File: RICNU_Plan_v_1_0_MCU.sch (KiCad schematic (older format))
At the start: 63 parts, among them SW3 SW_Push, U8 STM32F103RC, Y1 Crystal

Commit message: Re-routed CAN, RS-485, and debug connectors (wrong polarity in all)
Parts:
- removed SW3: SW_Push, Buttons_Switches_SMD:SW_SPST_KMR2, symbol SW_Push
- added SW3: SW_Push_4pin, RICNU_Plan_v_1_0:SW_SPST_KMR7, symbol SW_Push_4pin
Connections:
- net GND: now also SW3.2
- net MCU.CAN.SHDN: now also U8.8 (PC0); no longer U8.60 (BOOT0)
- net MCU.CAN.STB: now also U8.60 (BOOT0); no longer U8.8 (PC0)
- net MCU_SWD_RESET: now also SW3.1
- no-connect marks 9 -> 11
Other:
- moved on the sheet: C15

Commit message: Added connections to monitor power, changed CANSTB MCU pin, moved LED pins around
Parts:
- added R92: 10k, Resistors_SMD:R_0402_NoSilk, symbol R
- added R93, R94: 180, Resistors_SMD:R_0402_NoSilk, symbol R
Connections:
- net GND: now also R92.2
- net MCU.CAN.STB: now also U8.9 (PC1); no longer U8.60 (BOOT0)
- net MCU.LED.1: now also U8.15 (PA1); no longer U8.9 (PC1)
- net MCU.LED.2: now also U8.26 (PB0); no longer U8.10 (PC2)
- net MCU.LED.3: now also U8.27 (PB1); no longer U8.11 (PC3)
- net MCU.LED.4: now also U8.28 (PB2); no longer U8.15 (PA1)
- net MCU_PWREN: now reaches U8.39 (PC8)
- net MCU_PWREN: now also R93.2
- net MCU_USBON: now reaches U8.40 (PC9)
- net MCU_USBON: now also R92.1, R94.2
- new net MCU.PWREN: R93.1
- new net MCU.USBON: R94.1
- no-connect marks 11 -> 9
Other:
- note added: "USB Power Status Inputs"
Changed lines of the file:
@@
 Text HLabel 1650 4650 0    60   Output ~ 0
 MCU.RS485.TX
-NoConn ~ 6450 3400
-NoConn ~ 4950 3500
-NoConn ~ 4950 3600
-NoConn ~ 4950 3700
 NoConn ~ 4950 3400
 NoConn ~ 4950 1100
-NoConn ~ 6450 3500
 Text HLabel 10650 5050 2    60   BiDi ~ 0
 MCU.PB11
@@
 Text Label 2750 5900 0    60   ~ 0
 MCU_CAN_STB
-Text Label 6850 1400 0    60   ~ 0
+Text Label 4550 1800 2    60   ~ 0
 MCU_CAN_STB
 Text Label 2750 6000 0    60   ~ 0
@@
 Text Notes 900  1150 0    60   ~ 0
 SPI to SD Card
-Text Label 4550 1800 2    60   ~ 0
+Text Label 4550 2400 2    60   ~ 0
 MCU_LED_1
-Text Label 4550 1900 2    60   ~ 0
+Text Label 4550 3500 2    60   ~ 0
 MCU_LED_2
-Text Label 4550 2000 2    60   ~ 0
+Text Label 4550 3600 2    60   ~ 0
 MCU_LED_3
-Text Label 4550 2400 2    60   ~ 0
+Text Label 4550 3700 2    60   ~ 0
 MCU_LED_4
 $Comp
@@
 Text Label 4550 3900 2    60   ~ 0
 MCU_DIO_PB11
-Text HLabel 10300 3000 2    60   Input ~ 0
+Text HLabel 10300 2550 2    60   Input ~ 0
 MCU.LED.1
-Text HLabel 10300 3100 2    60   Input ~ 0
+Text HLabel 10300 2650 2    60   Input ~ 0
 MCU.LED.2
-Text HLabel 10300 3200 2    60   Input ~ 0
+Text HLabel 10300 2750 2    60   Input ~ 0
 MCU.LED.3
-Text HLabel 10300 3300 2    60   Input ~ 0
+Text HLabel 10300 2850 2    60   Input ~ 0
 MCU.LED.4
 $Comp
@@
 Text Label 8450 5050 2    60   ~ 0
 MCU_DIO_PB11
-Text Label 9200 3000 2    60   ~ 0
+Text Label 9200 2550 2    60   ~ 0
 MCU_LED_1
-Text Label 9200 3100 2    60   ~ 0
+Text Label 9200 2650 2    60   ~ 0
 MCU_LED_2
-Text Label 9200 3200 2    60   ~ 0
+Text Label 9200 2750 2    60   ~ 0
 MCU_LED_3
-Text Label 9200 3300 2    60   ~ 0
+Text Label 9200 2850 2    60   ~ 0
 MCU_LED_4
 $Comp
@@
 Text Notes 11100 4600 2    60   ~ 0
 GPIO Breakout
-Text Notes 10850 2850 2    60   ~ 0
+Text Notes 10850 2400 2    60   ~ 0
 LED Controls
 Text Label 4950 1200 2    60   ~ 0
@@
 Wire Wire Line
 	4550 1800 4950 1800
-Wire Wire Line
-	4550 1900 4950 1900
-Wire Wire Line
-	4550 2000 4950 2000
 Wire Notes Line
 	10500 1450 10500 2100
@@
 	10500 6250 10650 6250
 Wire Wire Line
-	10300 3000 9200 3000
-Wire Wire Line
-	10300 3100 9200 3100
-Wire Wire Line
-	10300 3200 9200 3200
-Wire Wire Line
-	10300 3300 9200 3300
+	10300 2550 9200 2550
+Wire Wire Line
+	10300 2650 9200 2650
+Wire Wire Line
+	10300 2750 9200 2750
+Wire Wire Line
+	10300 2850 9200 2850
 Wire Wire Line
 	8500 4400 8500 4250
@@
 Wire Wire Line
 	9850 4400 9850 4250
-Wire Wire Line
-	6450 1400 6850 1400
 Wire Wire Line
 	4550 2400 4950 2400
@@
 NoConn ~ 4900 5600
 NoConn ~ 4900 5200
+NoConn ~ 6450 1400
+Wire Wire Line
+	4950 3500 4550 3500
+Wire Wire Line
+	4950 3600 4550 3600
+Wire Wire Line
+	4950 3700 4550 3700
+NoConn ~ 4950 1900
+NoConn ~ 4950 2000
+Wire Wire Line
+	6450 3500 6850 3500
+Text Label 6850 3500 0    60   ~ 0
+MCU_PWREN
+Text Label 9200 3200 2    60   ~ 0
+MCU_PWREN
+Text HLabel 10300 3200 2    60   Input ~ 0
+MCU.PWREN
+Text Notes 10850 3100 2    60   ~ 0
+USB Power Status Inputs
+$Comp
+L R R93
+U 1 1 5A214822
+P 9750 3200
+F 0 "R93" V 9800 3400 50  0000 C CNN
+F 1 "180" V 9750 3200 50  0000 C CNN
+F 2 "Resistors_SMD:R_0402_NoSilk" V 9680 3200 50  0001 C CNN
+F 3 "" H 9750 3200 50  0001 C CNN
+	1    9750 3200
+	0    1    1    0
+$EndComp
+Wire Wire Line
+	9900 3200 10300 3200
+Wire Wire Line
+	9600 3200 9200 3200
+Text HLabel 10300 3300 2    60   Input ~ 0
+MCU.USBON
+Wire Wire Line
+	10300 3300 9900 3300
+$Comp
+L R R94
+U 1 1 5A2157A3
+P 9750 3300
+F 0 "R94" V 9800 3500 50  0000 C CNN
+F 1 "180" V 9750 3300 50  0000 C CNN
+F 2 "Resistors_SMD:R_0402_NoSilk" V 9680 3300 50  0001 C CNN
+F 3 "" H 9750 3300 50  0001 C CNN
+	1    9750 3300
+	0    1    1    0
+$EndComp
+Wire Wire Line
+	9600 3300 9200 3300
+Text Label 6850 3400 0    60   ~ 0
+MCU_USBON
+Wire Wire Line
+	6450 3400 6850 3400
+$Comp
+L R R92
+U 1 1 5A216900
+P 9400 3550
+F 0 "R92" V 9450 3750 50  0000 C CNN
+F 1 "10k" V 9400 3550 50  0000 C CNN
+F 2 "Resistors_SMD:R_0402_NoSilk" V 9330 3550 50  0001 C CNN
+F 3 "" H 9400 3550 50  0001 C CNN
+	1    9400 3550
+	1    0    0    -1
+$EndComp
+Wire Wire Line
+	9400 3400 9400 3300
+Connection ~ 9400 3300
+Wire Wire Line
+	9400 3700 9400 3800
+$Comp
+L GND #PWR057
+U 1 1 5A217257
+P 9400 3800
+F 0 "#PWR057" H 9400 3550 50  0001 C CNN
+F 1 "GND" H 9400 3650 50  0000 C CNN
+F 2 "" H 9400 3800 50  0001 C CNN
+F 3 "" H 9400 3800 50  0001 C CNN
+	1    9400 3800
+	-1   0    0    -1
+$EndComp
+Text Label 9200 3300 2    60   ~ 0
+MCU_USBON
 $EndSCHEMATC

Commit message: Design freeze - ordered the board
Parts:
- added R96, R99: 470, Resistors_SMD:R_0402_NoSilk, symbol R
- added R97, R98: 10k, Resistors_SMD:R_0402_NoSilk, symbol R
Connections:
- net +3V3: now also R97.1, R98.1
- net GND: now also R96.2, R99.2
- net MCU.LED.1: now also U8.25 (PC5); no longer U8.15 (PA1)
- net MCU.LED.4: now also U8.15 (PA1); no longer U8.28 (PB2)
- net MCU_BOOT0: now reaches U8.60 (BOOT0)
- net MCU_BOOT0: now also R98.2, R99.1
- new net MCU_BOOT1: R96.1, R97.2, U8.28 (PB2)
- no-connect marks 9 -> 7
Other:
- note added: "DNP"
- moved on the sheet: C13, C14, Y1
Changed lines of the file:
@@
 L Crystal Y1
 U 1 1 59D7EC04
-P 4200 1100
-F 0 "Y1" H 4200 1250 50  0000 C CNN
-F 1 "Crystal" H 4200 950 50  0000 C CNN
-F 2 "Crystals:Crystal_SMD_3215-2pin_3.2x1.5mm" H 4200 1100 50  0001 C CNN
-F 3 "" H 4200 1100 50  0001 C CNN
-	1    4200 1100
+P 4100 1100
+F 0 "Y1" H 4100 1250 50  0000 C CNN
+F 1 "Crystal" H 4100 950 50  0000 C CNN
+F 2 "Crystals:Crystal_SMD_3215-2pin_3.2x1.5mm" H 4100 1100 50  0001 C CNN
+F 3 "" H 4100 1100 50  0001 C CNN
+	1    4100 1100
 	0    1    1    0
 $EndComp
@@
 L C C13
 U 1 1 59D7EC93
-P 4000 900
-F 0 "C13" H 4025 1000 50  0000 L CNN
-F 1 "7p" H 4025 800 50  0000 L CNN
-F 2 "Capacitors_SMD:C_0402_NoSilk" H 4038 750 50  0001 C CNN
-F 3 "" H 4000 900 50  0001 C CNN
-	1    4000 900
+P 3900 900
+F 0 "C13" H 3925 1000 50  0000 L CNN
+F 1 "7p" H 3925 800 50  0000 L CNN
+F 2 "Capacitors_SMD:C_0402_NoSilk" H 3938 750 50  0001 C CNN
+F 3 "" H 3900 900 50  0001 C CNN
+	1    3900 900
 	0    1    1    0
 $EndComp
@@
 L C C14
 U 1 1 59D7ECF9
-P 4000 1300
-F 0 "C14" H 4025 1400 50  0000 L CNN
-F 1 "7p" H 4025 1200 50  0000 L CNN
-F 2 "Capacitors_SMD:C_0402_NoSilk" H 4038 1150 50  0001 C CNN
-F 3 "" H 4000 1300 50  0001 C CNN
-	1    4000 1300
+P 3900 1300
+F 0 "C14" H 3925 1400 50  0000 L CNN
+F 1 "7p" H 3925 1200 50  0000 L CNN
+F 2 "Capacitors_SMD:C_0402_NoSilk" H 3938 1150 50  0001 C CNN
+F 3 "" H 3900 1300 50  0001 C CNN
+	1    3900 1300
 	0    1    1    0
 $EndComp
@@
 Text HLabel 1650 4650 0    60   Output ~ 0
 MCU.RS485.TX
-NoConn ~ 4950 3400
 NoConn ~ 4950 1100
 Text HLabel 10650 5050 2    60   BiDi ~ 0
@@
 L GND #PWR042
 U 1 1 59DE2264
-P 3700 1200
-F 0 "#PWR042" H 3700 950 50  0001 C CNN
-F 1 "GND" H 3700 1050 50  0000 C CNN
-F 2 "" H 3700 1200 50  0001 C CNN
-F 3 "" H 3700 1200 50  0001 C CNN
-	1    3700 1200
+P 3600 1200
+F 0 "#PWR042" H 3600 950 50  0001 C CNN
+F 1 "GND" H 3600 1050 50  0000 C CNN
+F 2 "" H 3600 1200 50  0001 C CNN
+F 3 "" H 3600 1200 50  0001 C CNN
+	1    3600 1200
 	1    0    0    -1
 $EndComp
@@
 Text Notes 900  1150 0    60   ~ 0
 SPI to SD Card
-Text Label 4550 2400 2    60   ~ 0
+Text Label 4550 3400 2    60   ~ 0
 MCU_LED_1
 Text Label 4550 3500 2    60   ~ 0
@@
 Text Label 4550 3600 2    60   ~ 0
 MCU_LED_3
-Text Label 4550 3700 2    60   ~ 0
+Text Label 4550 2400 2    60   ~ 0
 MCU_LED_4
 $Comp
@@
 Text Notes 10850 2400 2    60   ~ 0
 LED Controls
-Text Label 4950 1200 2    60   ~ 0
+Text Label 4400 1200 0    60   ~ 0
 OSC32_IN
-Text Label 4950 1300 2    60   ~ 0
+Text Label 4400 1300 0    60   ~ 0
 OSC32_OUT
 Text Label 8650 1650 0    60   ~ 0
@@
 Text Label 6850 1000 0    60   ~ 0
 MCU_VCC
-Text Label 4550 750  2    60   ~ 0
+Text Label 4400 1000 0    60   ~ 0
 MCU_VCC
 Text Label 6850 2600 0    60   ~ 0
@@
 Connection ~ 10350 2050
 Wire Wire Line
-	3800 1300 3850 1300
-Wire Wire Line
-	3850 900  3800 900
-Wire Wire Line
-	4150 900  4450 900
-Wire Wire Line
-	4200 900  4200 950
-Wire Wire Line
-	4200 1300 4200 1250
-Connection ~ 4200 900
-Connection ~ 4200 1300
+	3700 1300 3750 1300
+Wire Wire Line
+	3750 900  3700 900
+Wire Wire Line
+	4050 900  4350 900
+Wire Wire Line
+	4100 900  4100 950
+Wire Wire Line
+	4100 1300 4100 1250
+Connection ~ 4100 900
+Connection ~ 4100 1300
 Wire Wire Line
 	6450 2500 6850 2500
@@
 	4550 1600 4950 1600
 Wire Wire Line
-	3800 900  3800 1300
-Connection ~ 3800 1100
-Wire Wire Line
-	4150 1300 4950 1300
-Wire Wire Line
-	4450 1200 4950 1200
+	3700 900  3700 1300
+Connection ~ 3700 1100
+Wire Wire Line
+	4050 1300 4950 1300
+Wire Wire Line
+	4350 1200 4950 1200
 Wire Wire Line
 	6850 2400 6450 2400
@@
 	4550 3900 4950 3900
 Wire Wire Line
-	3700 1200 3700 1100
-Wire Wire Line
-	3700 1100 3800 1100
+	3600 1200 3600 1100
+Wire Wire Line
+	3600 1100 3700 1100
 Wire Wire Line
 	6850 3300 6450 3300
 Wire Wire Line
-	4450 900  4450 1200
+	4350 900  4350 1200
 Wire Wire Line
 	2200 1300 2650 1300
@@
 Wire Wire Line
 	9850 4400 9850 4250
-Wire Wire Line
-	4550 2400 4950 2400
 $Comp
 L SW_Push_4pin SW3
@@
 $EndComp
 Wire Wire Line
-	4550 750  4550 1000
-Wire Wire Line
-	4550 1000 4950 1000
+	4400 1000 4950 1000
 $Comp
 L PWR_FLAG #FLG057
@@
 NoConn ~ 4900 5600
 NoConn ~ 4900 5200
-NoConn ~ 6450 1400
 Wire Wire Line
 	4950 3500 4550 3500
@@
 $EndComp
 Wire Wire Line
-	9600 3300 9200 3300
+	9200 3300 9600 3300
 Text Label 6850 3400 0    60   ~ 0
 MCU_USBON
@@
 Text Label 9200 3300 2    60   ~ 0
 MCU_USBON
+Wire Wire Line
+	4550 3400 4950 3400
+Text Label 6850 1400 0    60   ~ 0
+MCU_BOOT0
+Text Label 4550 3700 2    60   ~ 0
+MCU_BOOT1
+Wire Wire Line
+	6450 1400 6850 1400
+Wire Wire Line
+	5500 6700 5500 6800
+$Comp
+L GND #PWR059
+U 1 1 5A25E35E
+P 5500 7150
+F 0 "#PWR059" H 5500 6900 50  0001 C CNN
+F 1 "GND" H 5500 7000 50  0000 C CNN
+F 2 "" H 5500 7150 50  0001 C CNN
+F 3 "" H 5500 7150 50  0001 C CNN
+	1    5500 7150
+	1    0    0    -1
+$EndComp
+Wire Wire Line
+	5500 7150 5500 7100
+$Comp
+L R R99
+U 1 1 5A25E365
+P 5500 6950
+F 0 "R99" V 5600 6950 50  0000 C CNN
+F 1 "470" V 5500 6950 50  0000 C CNN
+F 2 "Resistors_SMD:R_0402_NoSilk" V 5430 6950 50  0001 C CNN
+F 3 "" H 5500 6950 50  0001 C CNN
+	1    5500 6950
+	1    0    0    -1
+$EndComp
+Wire Wire Line
+	4500 6750 4350 6750
+Text Label 4350 6750 2    60   ~ 0
+MCU_BOOT1
+Text Label 5350 6750 2    60   ~ 0
+MCU_BOOT0
+Wire Wire Line
+	5350 6750 5500 6750
+$Comp
+L GND #PWR060
+U 1 1 5A25974F
+P 4500 7150
+F 0 "#PWR060" H 4500 6900 50  0001 C CNN
+F 1 "GND" H 4500 7000 50  0000 C CNN
+F 2 "" H 4500 7150 50  0001 C CNN
+F 3 "" H 4500 7150 50  0001 C CNN
+	1    4500 7150
+	1    0    0    -1
+$EndComp
+Wire Wire Line
+	4500 7150 4500 7100
+$Comp
+L R R96
+U 1 1 5A25A976
+P 4500 6950
+F 0 "R96" V 4600 6950 50  0000 C CNN
+F 1 "470" V 4500 6950 50  0000 C CNN
+F 2 "Resistors_SMD:R_0402_NoSilk" V 4430 6950 50  0001 C CNN
+F 3 "" H 4500 6950 50  0001 C CNN
+	1    4500 6950
+	1    0    0    -1
+$EndComp
+$Comp
+L R R98
+U 1 1 5A260571
+P 5500 6550
+F 0 "R98" V 5600 6550 50  0000 C CNN
+F 1 "10k" V 5500 6550 50  0000 C CNN
+F 2 "Resistors_SMD:R_0402_NoSilk" V 5430 6550 50  0001 C CNN
+F 3 "" H 5500 6550 50  0001 C CNN
+	1    5500 6550
+	1    0    0    -1
+$EndComp
+Connection ~ 5500 6750
+Wire Wire Line
+	4500 6700 4500 6800
+$Comp
+L +3V3 #PWR061
+U 1 1 5A260CED
+P 5500 6350
+F 0 "#PWR061" H 5500 6200 50  0001 C CNN
+F 1 "+3V3" H 5500 6490 50  0000 C CNN
+F 2 "" H 5500 6350 50  0001 C CNN
+F 3 "" H 5500 6350 50  0001 C CNN
+	1    5500 6350
+	1    0    0    -1
+$EndComp
+Wire Wire Line
+	5500 6400 5500 6350
+Text Notes 5250 6550 0    60   ~ 0
+DNP
+$Comp
+L R R97
+U 1 1 5A2648A3
+P 4500 6550
+F 0 "R97" V 4600 6550 50  0000 C CNN
+F 1 "10k" V 4500 6550 50  0000 C CNN
+F 2 "Resistors_SMD:R_0402_NoSilk" V 4430 6550 50  0001 C CNN
+F 3 "" H 4500 6550 50  0001 C CNN
+	1    4500 6550
+	1    0    0    -1
+$EndComp
+Connection ~ 4500 6750
+$Comp
+L +3V3 #PWR062
+U 1 1 5A264B39
+P 4500 6350
+F 0 "#PWR062" H 4500 6200 50  0001 C CNN
+F 1 "+3V3" H 4500 6490 50  0000 C CNN
+F 2 "" H 4500 6350 50  0001 C CNN
+F 3 "" H 4500 6350 50  0001 C CNN
+	1    4500 6350
+	1    0    0    -1
+$EndComp
+Wire Wire Line
+	4500 6350 4500 6400
+Wire Wire Line
+	4950 2400 4550 2400
+Text Notes 4250 6550 0    60   ~ 0
+DNP
 $EndSCHEMATC

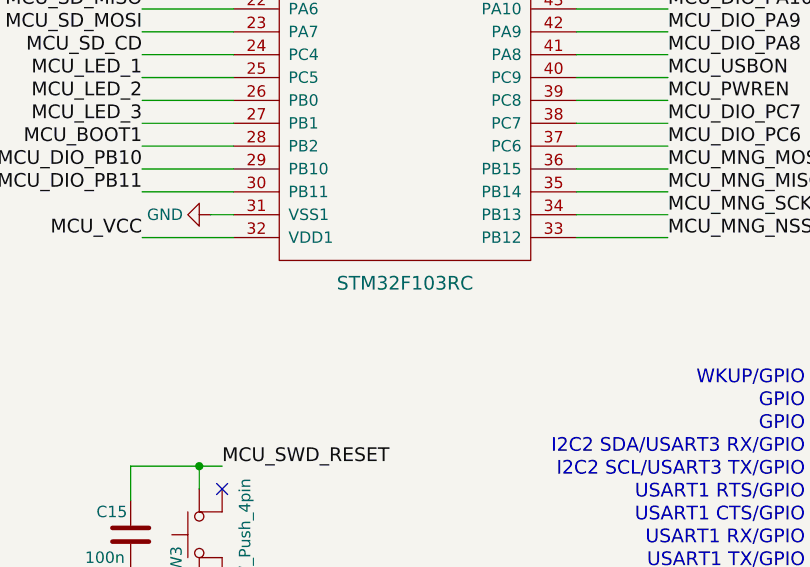
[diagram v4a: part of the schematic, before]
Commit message: Various small changes like comment removal
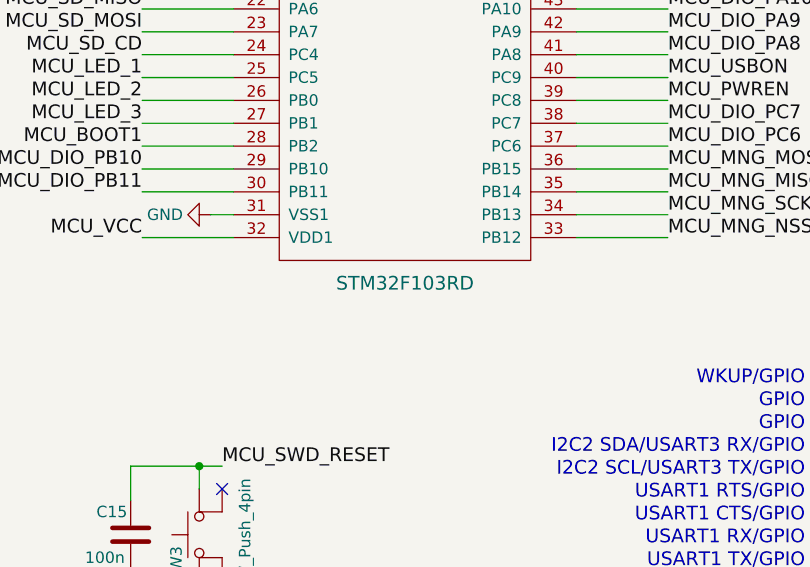
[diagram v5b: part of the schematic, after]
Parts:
- U8: value STM32F103RC -> STM32F103RD
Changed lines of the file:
@@
 P 5700 2550
 F 0 "U8" H 5200 4300 60  0000 C CNN
-F 1 "STM32F103RC" H 5700 800 60  0000 C CNN
+F 1 "STM32F103RD" H 5700 800 60  0000 C CNN
 F 2 "Housings_QFP:TQFP-64_10x10mm_Pitch0.5mm" H 5700 2650 60  0001 C CNN
 F 3 "" H 5700 2650 60  0001 C CNN
